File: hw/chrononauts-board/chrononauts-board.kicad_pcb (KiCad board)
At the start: 2 copper layers, 54 x 21.9 mm, 45 parts, among them IC1 ESP32-C3-WROOM-02-N4, IC2 TLV62568DBVR, J1 73251-1290, J2 USB4105-GF-A, U1 CC1101RGP, Y1 NX3225GA-26MHZ

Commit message: hw: generate fab outputs
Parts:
- C1, C10, C11, C12, C13, C14, C15, C16, C17, C18, C19, C2, C20, C21, C3, C4, C5, C6, C7, C8, C9: footprint ChrononautsLib:Cap_Murata_GRM_0402 -> PCBLib:Cap_Murata_GRM_0402
- C22: footprint ChrononautsLib:Cap_Murata_GRM_0603 -> PCBLib:Cap_Murata_GRM_0603
- D1, D2, D3: footprint ChrononautsLib:SODFL1006X40N -> PCBLib:SODFL1006X40N
- D4: value B5819W-TP -> D4; footprint ChrononautsLib:SOD3716X135N -> PCBLib:SOD3716X135N
- IC1: footprint ChrononautsLib:ESP32C3WROOM02N4 -> PCBLib:ESP32C3WROOM02N4
- IC2: footprint ChrononautsLib:TLV62568DBVR -> PCBLib:TLV62568DBVR
- J1: footprint ChrononautsLib:Molex-SD-73251-129 -> PCBLib:Molex-SD-73251-129
- J2: value USB4105-GF-A -> J2; footprint ChrononautsLib:GCT_USB4105-GF-A -> PCBLib:GCT_USB4105-GF-A
- L1, L2, L3, L4: footprint ChrononautsLib:L_Murata_LQG_0402 -> PCBLib:L_Murata_LQG_0402
- L5: footprint ChrononautsLib:ASPI0418FS -> PCBLib:ASPI0418FS
- R1: footprint ChrononautsLib:R_KOA_RK_0402 -> PCBLib:R_KOA_RK_0402
- R2, R3, R4, R5, R8: footprint ChrononautsLib:R_Vishay_CRCW_0402 -> PCBLib:R_Vishay_CRCW_0402
- R6, R7: footprint ChrononautsLib:R_Bourns_CR_0603 -> PCBLib:R_Bourns_CR_0603
- U1: value CC1101RGP -> ${REFERENCE}; footprint ChrononautsLib:CC1101RGP -> PCBLib:CC1101RGP
- Y1: footprint ChrononautsLib:NX3225GA16000MSTDCRG1 -> PCBLib:NX3225GA16000MSTDCRG1

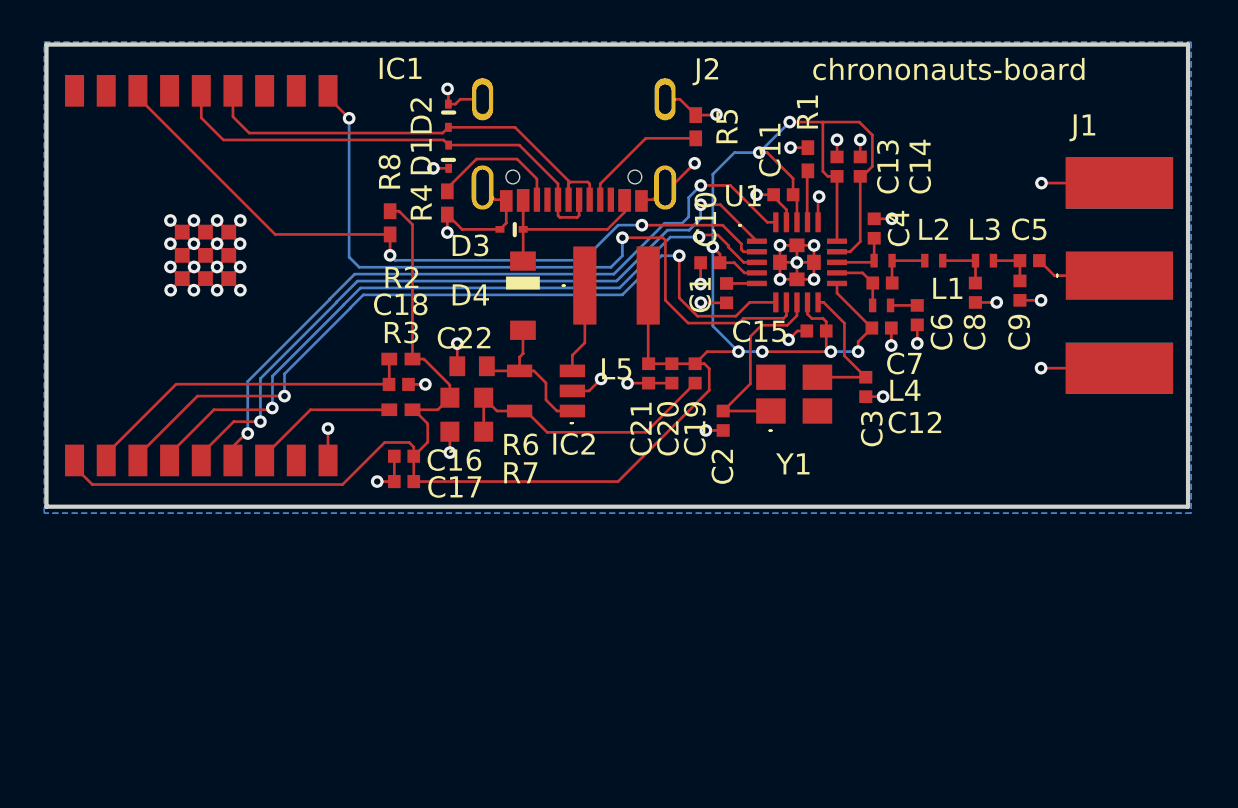
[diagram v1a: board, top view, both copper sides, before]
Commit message: add LEDs, push button, potentiometer and I2C accelerometer (preliminary)
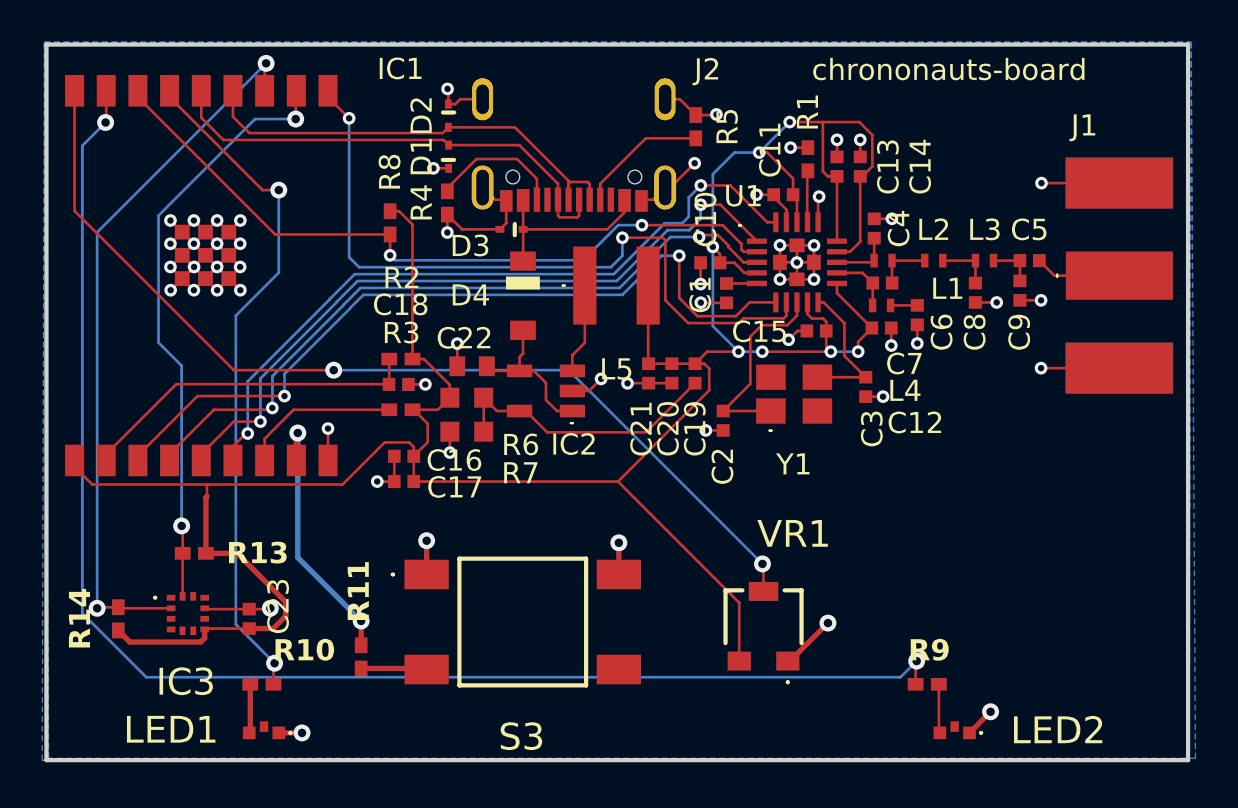
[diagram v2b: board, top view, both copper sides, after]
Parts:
- added C23: 1uF, PCBLib:Cap_Murata_GRM_0402, F.Cu at (107.9, 75.3)
- added IC3: MXC6655XA, PCBLib:MXC6655XA, F.Cu at (105.0, 75.0)
- added LED1: 155060VS73200, PCBLib:155060VS73200, F.Cu at (108.6, 80.7)
- added LED2: 155060VS73200, PCBLib:155060VS73200, F.Cu at (141.3, 80.7)
- added R10: 174, PCBLib:R_Vishay_CRCW_0402, F.Cu at (108.5, 78.4)
- added R11: 174, PCBLib:R_Vishay_CRCW_0402, F.Cu at (113.2, 77.1)
- added R13: 2K7, PCBLib:R_Vishay_CRCW_0402, F.Cu at (105.3, 72.2)
- added R14: 2K7, PCBLib:R_Vishay_CRCW_0402, F.Cu at (101.7, 75.3)
- added R9: 174, PCBLib:R_Vishay_CRCW_0402, F.Cu at (140.0, 78.4)
- added S3: 2-1977223-8, PCBLib:219772238, F.Cu at (120.8, 75.5)
- added VR1: PVG3A103C01R00, PCBLib:PVG3A103C01R00, F.Cu at (132.2, 75.7)
- D4: value D4 -> B5819W-TP
- J2: value J2 -> USB4105-GF-A
- U1: value ${REFERENCE} -> CC1101RGP
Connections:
- IC1 pad 11: unconnected-(IC1-GPIO20/U0RXD-Pad11) -> SCL
- IC1 pad 12: unconnected-(IC1-GPIO21/U0TXD-Pad12) -> SDA
- IC1 pad 15: unconnected-(IC1-IO3-Pad15) -> LED1
- IC1 pad 17: unconnected-(IC1-GPIO1/XTALN-Pad17) -> LED2
- IC1 pad 18: unconnected-(IC1-GPIO0/XTALP-Pad18) -> POTI
- IC1 pad 8: unconnected-(IC1-IO9-Pad8) -> BTN1
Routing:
- net LED2: track 0.00 -> 67.4 mm, vias 0 -> 2
- net POTI: track 0.00 -> 46.5 mm, vias 0 -> 2
- net SDA: track 0.00 -> 34.0 mm, vias 0 -> 2
- net LED1: track 0.00 -> 32.3 mm, vias 0 -> 2
- net +3V3: track 111.0 -> 139.5 mm
- net SCL: track 0.00 -> 28.2 mm, vias 0 -> 2
- net BTN1: track 0.00 -> 12.6 mm, vias 0 -> 2
- net Earth: track 86.3 -> 97.7 mm, vias 50 -> 56
- net Net-(S3-NO_1): track 0.00 -> 3.12 mm
- net Net-(LED1-A): track 0.00 -> 2.32 mm
- net Net-(LED2-A): track 0.00 -> 2.32 mm
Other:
- board size 54 x 21.9 mm -> 54 x 33.9 mm

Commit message: ready for production
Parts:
- added H1: MountingHole_Pad, MountingHole:MountingHole_2.2mm_M2_DIN965_Pad_TopBottom, F.Cu at (149.8, 50.6)
- added H2: MountingHole_Pad, MountingHole:MountingHole_2.2mm_M2_DIN965_Pad_TopBottom, F.Cu at (149.9, 79.5)
- added H4: MountingHole_Pad, MountingHole:MountingHole_2.2mm_M2_DIN965_Pad_TopBottom, F.Cu at (100.8, 79.5)
- moved R6 5.16 mm to (121.5, 68.8), turned to 180 degrees
- moved R7 3.39 mm to (121.5, 67.2), turned to 0 degrees
- moved R11 2.45 mm to (110.8, 77.1)
- moved S3 2.45 mm to (118.4, 75.5)
- moved C22 1.08 mm to (119.1, 64.2), turned to -90 degrees
- moved C20 1.07 mm to (126.8, 63.5)
- moved C21 1.07 mm to (125.8, 63.5)
- moved C19 1.07 mm to (128.0, 63.5)
- moved LED2 0.75 mm to (142.1, 80.7)
- moved R9 0.75 mm to (140.8, 78.4)
- moved R14 0.21 mm to (101.9, 75.3), turned to -90 degrees
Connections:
- net Net-(IC2-SW) renamed /SW
- R14 pad 1: +3V3 -> SDA
- R14 pad 2: SDA -> +3V3
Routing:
- net +3V3: track 139.5 -> 96.5 mm, vias 7 -> 9
- net POTI: track 46.5 -> 62.8 mm
- net /SW: track 4.28 -> 0.00 mm
- net Net-(IC2-FB): track 13.3 -> 17.3 mm, vias 0 -> 2
- net SDA: track 34.0 -> 30.1 mm
- net LED1: track 32.3 -> 36.0 mm
- net BTN1: track 12.6 -> 9.03 mm
- net Earth: track 97.7 -> 94.8 mm, vias 56 -> 60
- net MISO: track 34.8 -> 37.1 mm
- net SCL: track 28.2 -> 26.2 mm
- net LED2: track 67.4 -> 65.9 mm
- net USB_DN: track 22.1 -> 23.3 mm
- net +5V: track 7.40 -> 6.45 mm, vias 0 -> 2
- net USB_DP: track 22.8 -> 23.3 mm
- added copper zone on F.Cu, net +3V3
- added copper zone on F.Cu, net +5V
- added copper zone on F.Cu, net /SW
- added copper zone on F.Cu, net Earth

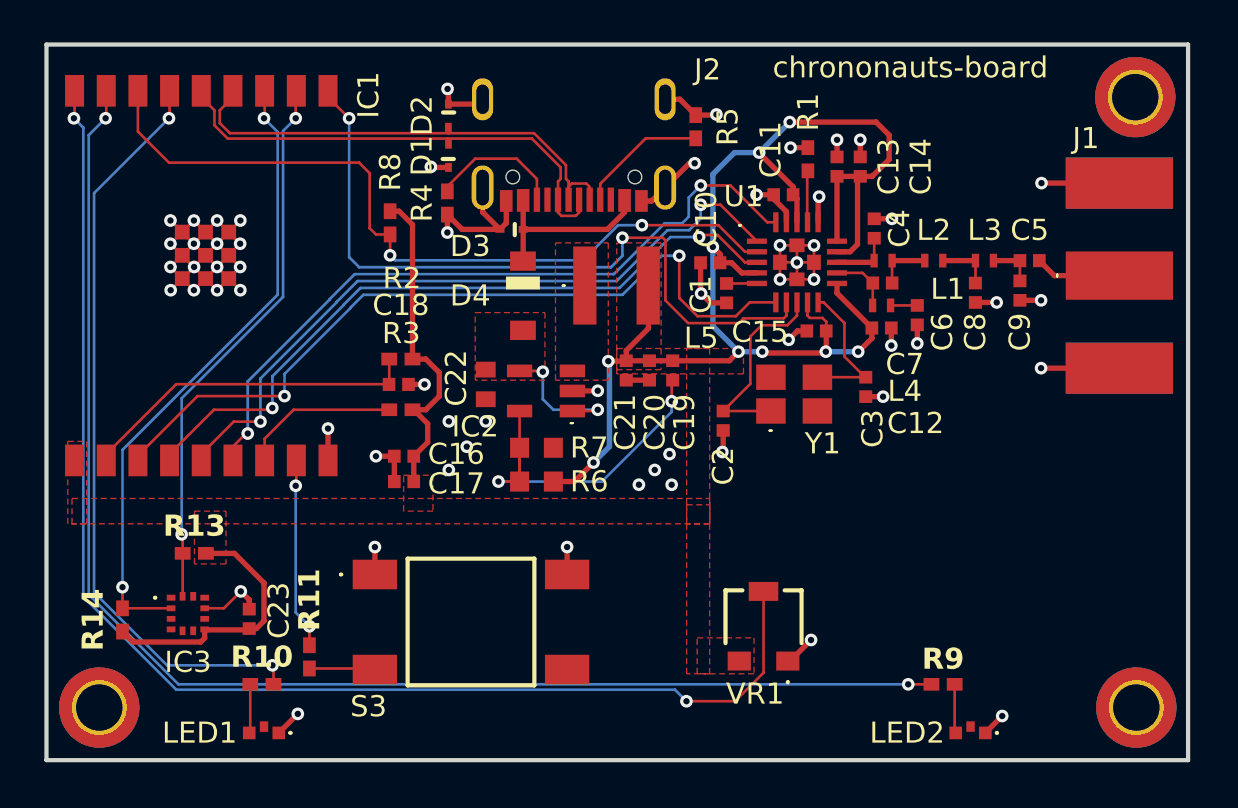
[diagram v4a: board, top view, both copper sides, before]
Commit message: HW: Update assembly and production data
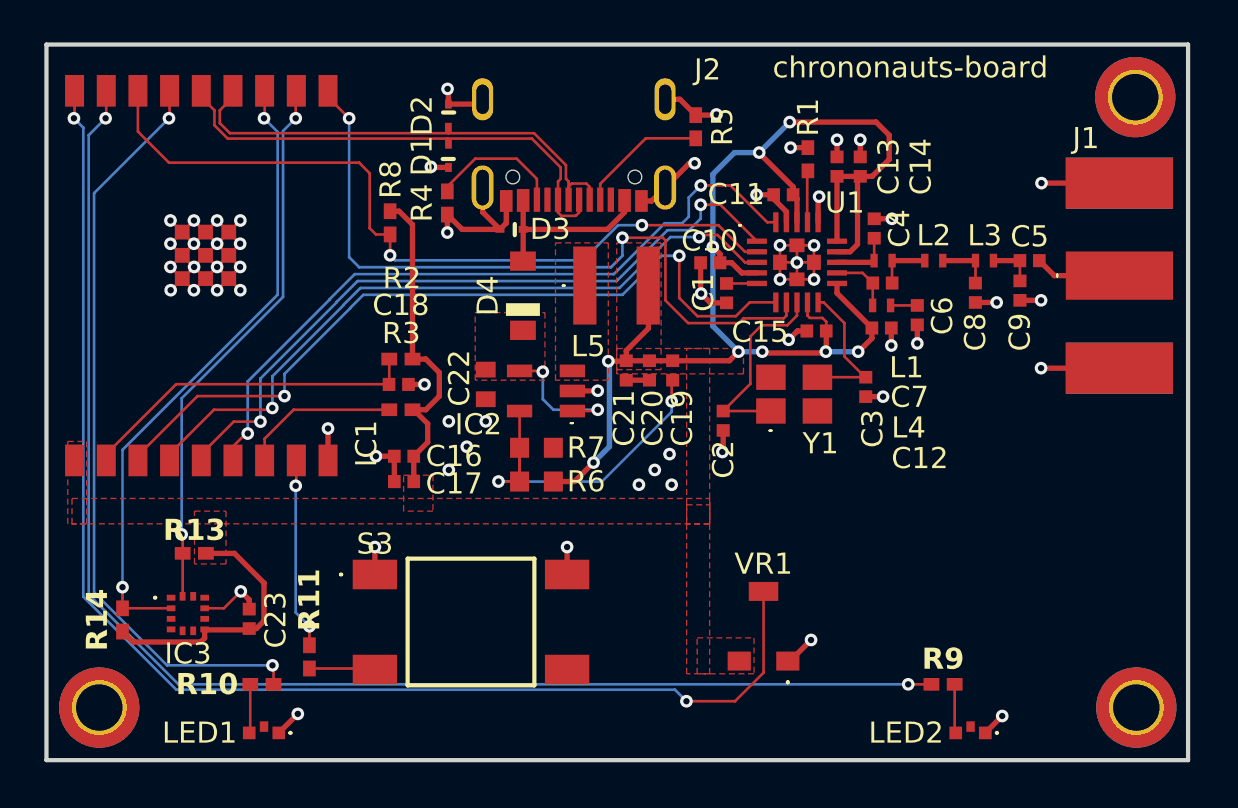
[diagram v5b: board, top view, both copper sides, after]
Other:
- board text added: "PCB ANTENNA"
